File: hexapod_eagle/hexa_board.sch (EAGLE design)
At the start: 38 parts

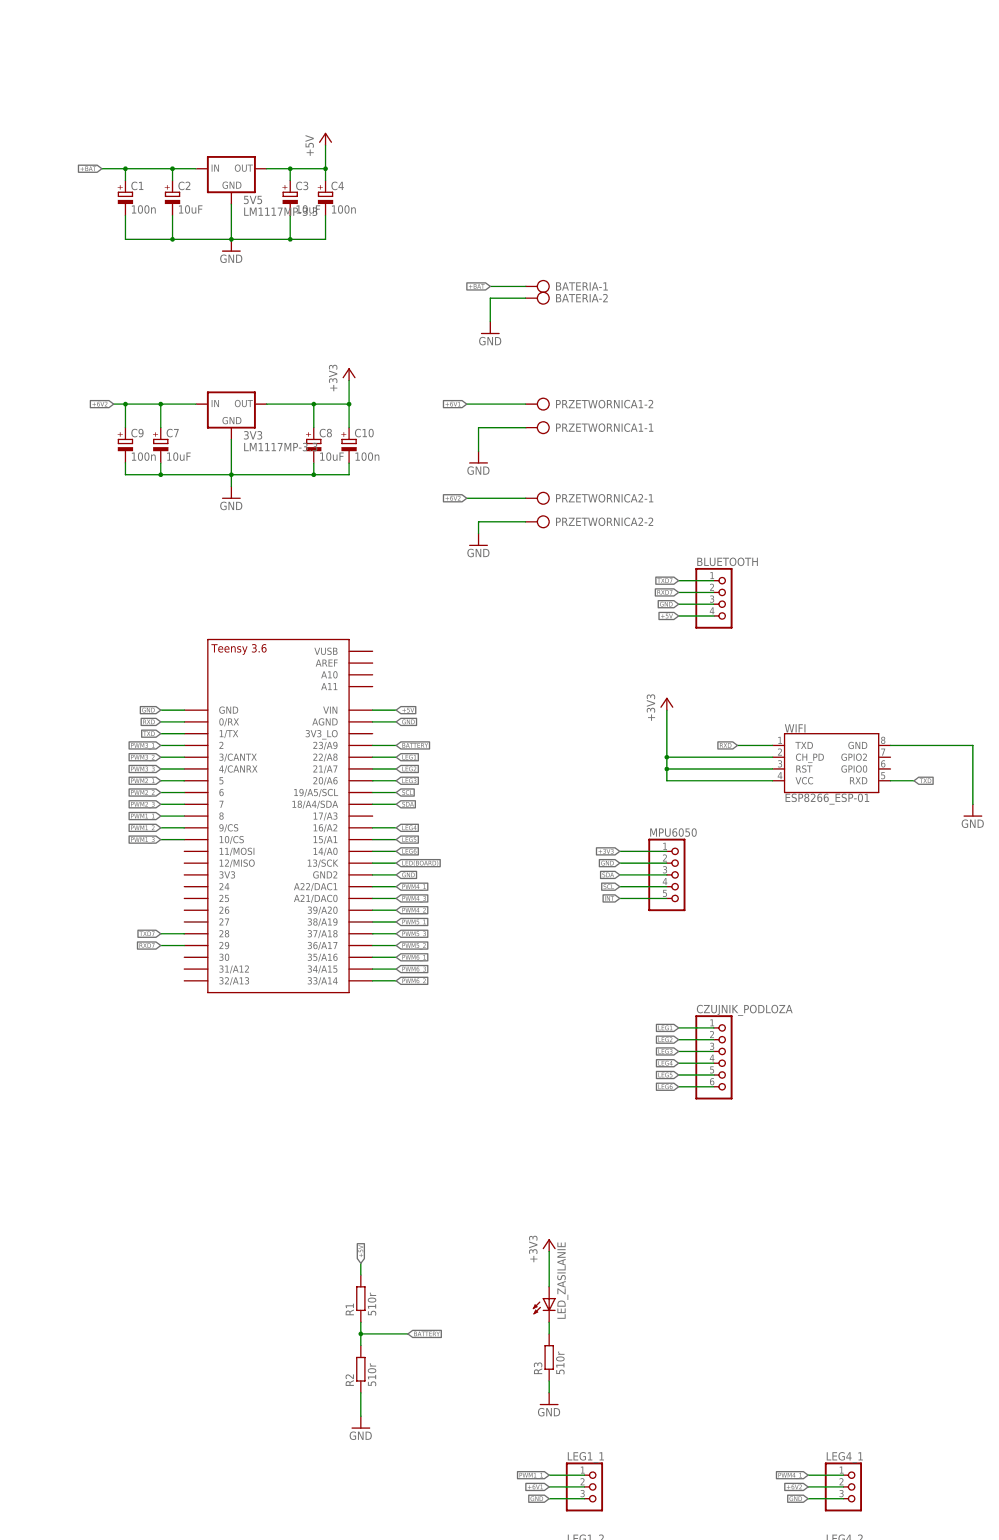
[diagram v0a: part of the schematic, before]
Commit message: Hexapod board v2
Changelog:
-new package for voltage regulator
-supply for ground sensor
-fix voltage sensor
-second battery voltage sensor
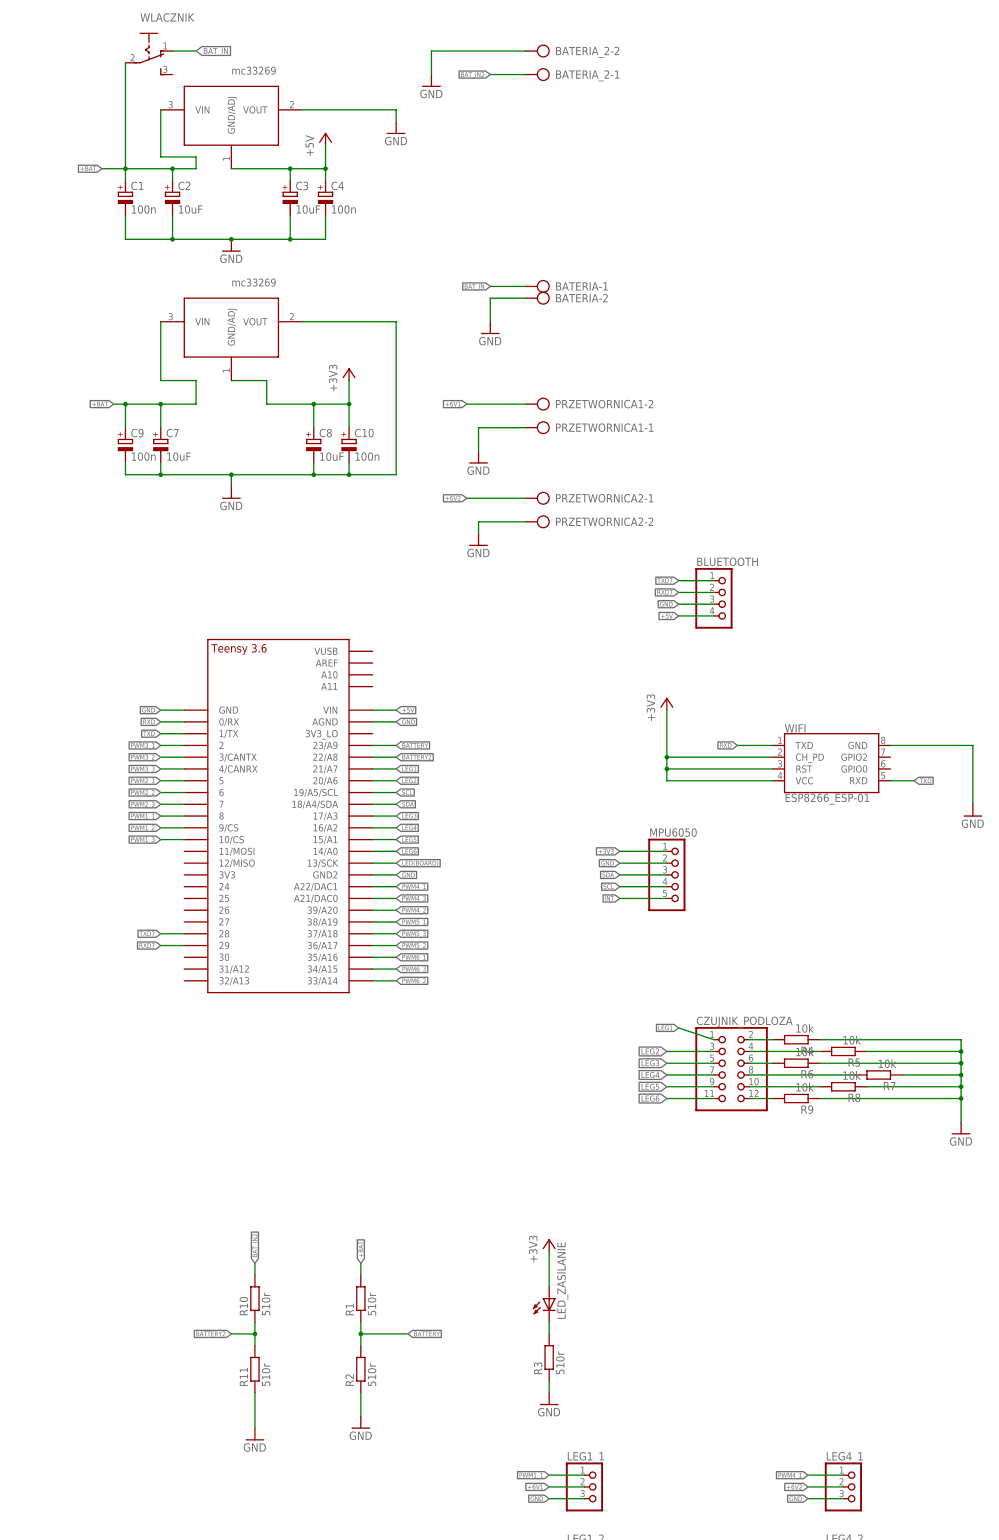
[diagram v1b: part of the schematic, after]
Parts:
- removed 3V3, 5V5: LM1117MP-3.3, lm1117_10:LM1117MP-3.3
- added 3V, 5V: MC33269, mc33269:MC33269
- added BATERIA_2: (no value), con-ptr500:AK300/2
- added R10, R11: 510r, rcl:R-EU_R0805
- added R4, R5, R6, R7, R8, R9: 10k, rcl:R-EU_R0805
- added WLACZNIK: (no value), switch:255SB
- CZUJNIK_PODLOZA: device pinhead:PINHD-1X6 -> pinhead:PINHD-2X6
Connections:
- new net BATTERY2: R10.1, R11.2, TEENSY41.22/A8
- new net BAT_IN: BATERIA-1.KL, WLACZNIK.O
- new net BAT_IN2: BATERIA_2-1.KL, R10.2
- new net N$1: CZUJNIK_PODLOZA.2, R4.2
- new net N$2: CZUJNIK_PODLOZA.4, R5.2
- new net N$3: CZUJNIK_PODLOZA.6, R6.2
- new net N$5: CZUJNIK_PODLOZA.8, R7.2
- new net N$6: CZUJNIK_PODLOZA.10, R8.2
- new net N$7: CZUJNIK_PODLOZA.12, R9.2
- net +3V3: now also 3V.GND/ADJ; no longer 3V3.OUT
- net +5V: now also 5V.GND/ADJ; no longer 5V5.OUT, R1.2
- net +6V2: no longer 3V3.IN, C7.+, C9.+
- net +BAT: now also 3V.VIN, 5V.VIN, C7.+, C9.+, R1.2, WLACZNIK.P; no longer 5V5.IN, BATERIA-1.KL
- net GND: now also 3V.VOUT, 5V.VOUT, BATERIA_2-2.KL, R11.1, R4.1, R5.1, R6.1, R7.1, R8.1, R9.1; no longer 3V3.GND, 5V5.GND
- net LEG1: now also TEENSY41.21/A7; no longer TEENSY41.22/A8
- net LEG2: now also CZUJNIK_PODLOZA.3, TEENSY41.20/A6; no longer CZUJNIK_PODLOZA.2, TEENSY41.21/A7
- net LEG3: now also CZUJNIK_PODLOZA.5, TEENSY41.17/A3; no longer CZUJNIK_PODLOZA.3, TEENSY41.20/A6
- net LEG4: now also CZUJNIK_PODLOZA.7; no longer CZUJNIK_PODLOZA.4
- net LEG5: now also CZUJNIK_PODLOZA.9; no longer CZUJNIK_PODLOZA.5
- net LEG6: now also CZUJNIK_PODLOZA.11; no longer CZUJNIK_PODLOZA.6

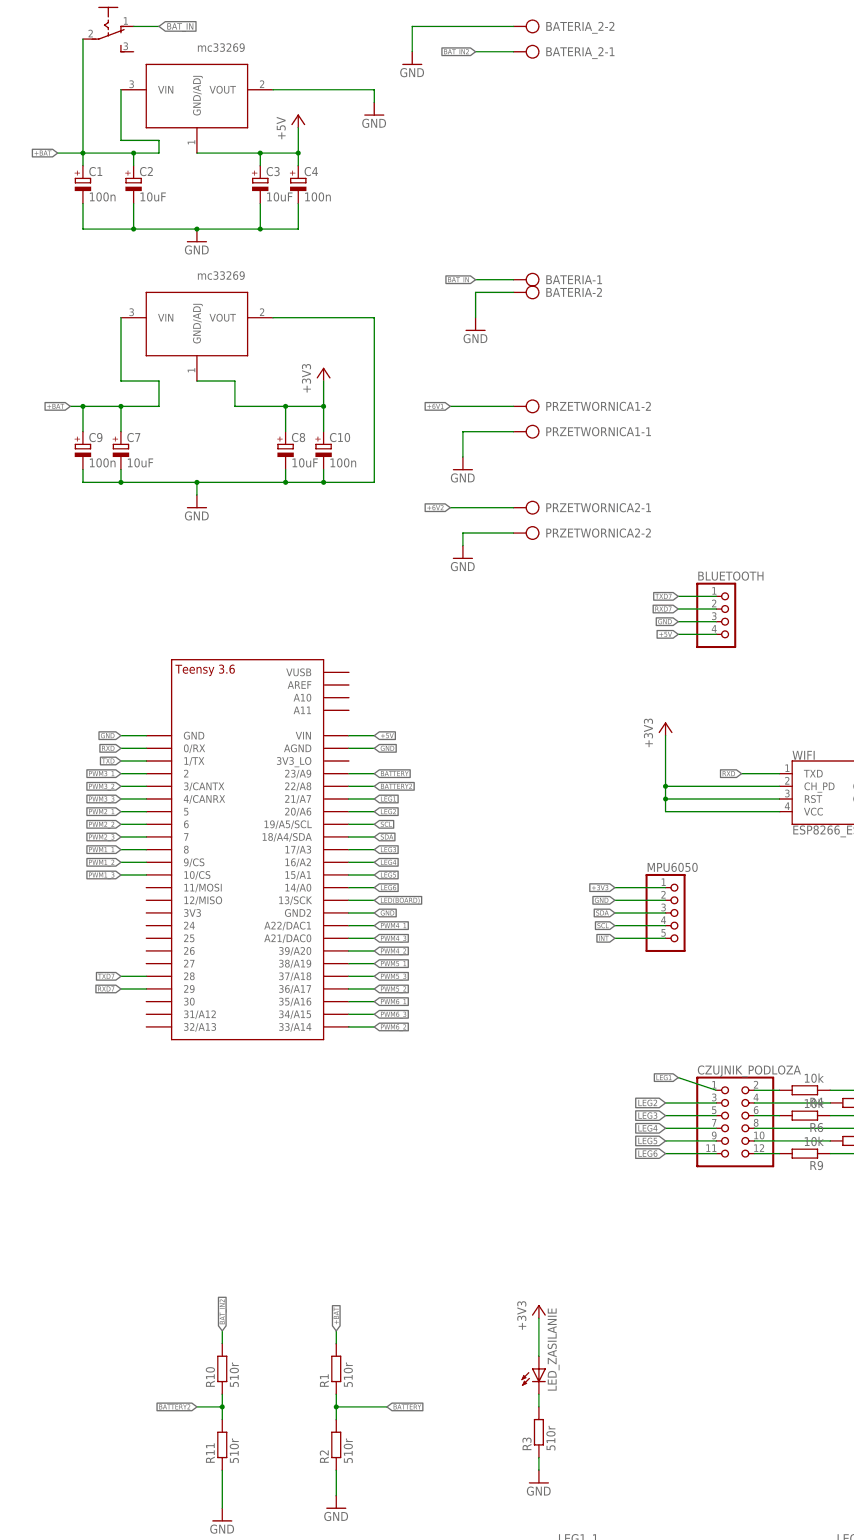
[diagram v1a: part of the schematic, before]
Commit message: Board v2
Changelog:
-on/off swich for power mcu(was in last update)
-add 2 leds for comunication
-some positions changes
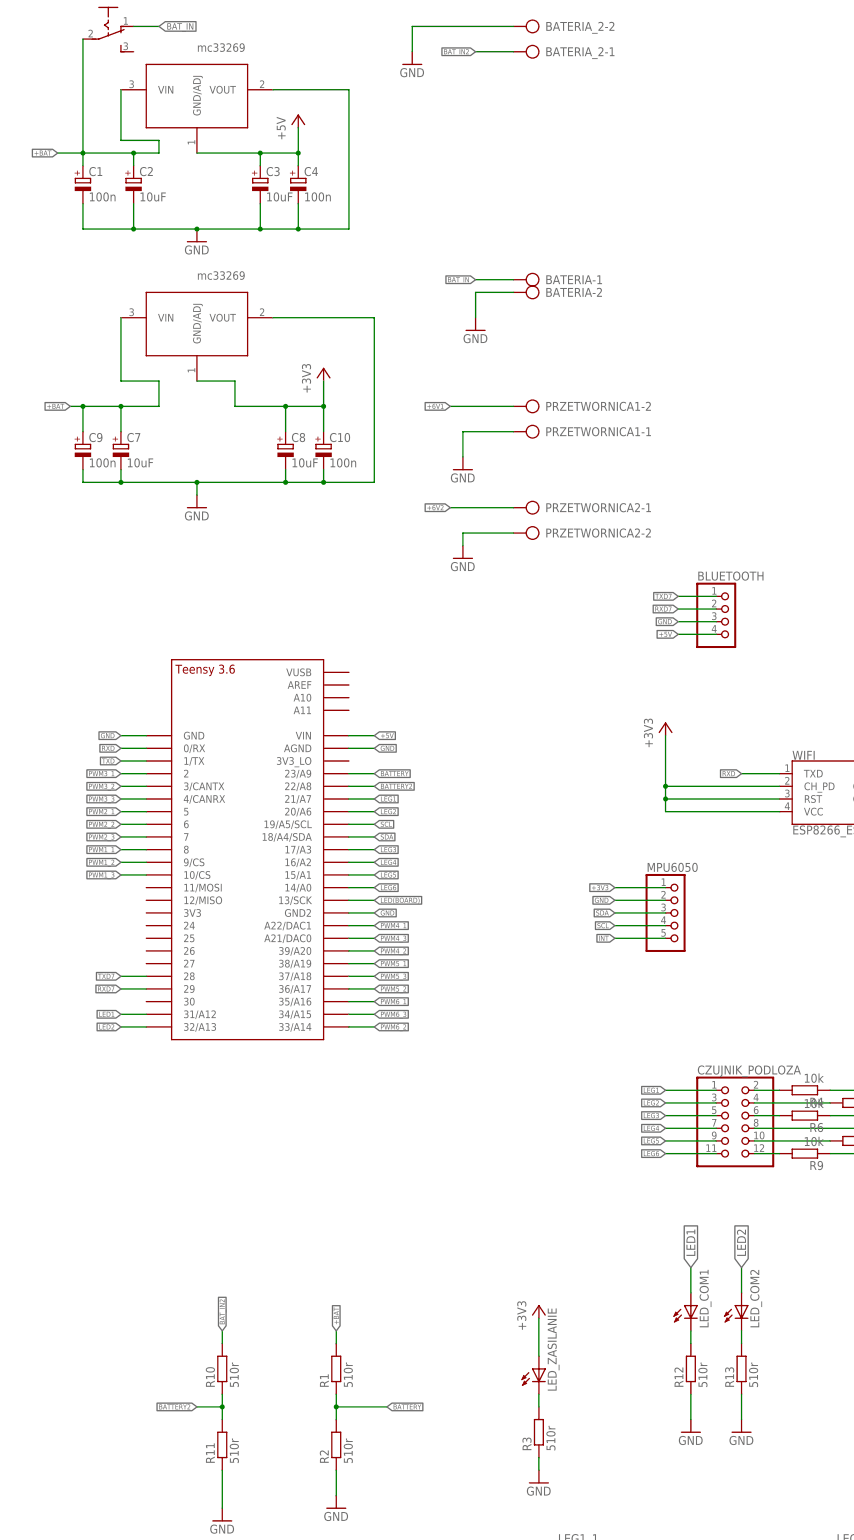
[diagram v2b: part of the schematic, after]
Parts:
- added LED_COM1, LED_COM2: (no value), led:LEDSML0805
- added R12, R13: 510r, rcl:R-EU_R0805
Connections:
- new net LED1: LED_COM1.A, TEENSY41.31/A12
- new net LED2: LED_COM2.A, TEENSY41.32/A13
- new net N$8: LED_COM1.C, R12.2
- new net N$9: LED_COM2.C, R13.2
- net GND: now also R12.1, R13.1
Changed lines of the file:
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@@
 <part name="GND7" library="supply1" deviceset="GND" device=""/>
 <part name="5V" library="mc33269" deviceset="MC33269" device=""/>
-<part name="GND9" library="supply1" deviceset="GND" device=""/>
 <part name="3V" library="mc33269" deviceset="MC33269" device=""/>
+<part name="R12" library="rcl" deviceset="R-EU_" device="R0805" value="510r"/>
+<part name="R13" library="rcl" deviceset="R-EU_" device="R0805" value="510r"/>
+<part name="LED_COM1" library="led" deviceset="LED" device="SML0805"/>
+<part name="LED_COM2" library="led" deviceset="LED" device="SML0805"/>
+<part name="GND10" library="supply1" deviceset="GND" device=""/>
+<part name="GND14" library="supply1" deviceset="GND" device=""/>
 </parts>
 <sheets>
@@
 <instance part="GND7" gate="1" x="30.48" y="-5.08"/>
 <instance part="5V" gate="G$1" x="27.94" y="271.78"/>
-<instance part="GND9" gate="1" x="60.96" y="276.86"/>
 <instance part="3V" gate="G$1" x="27.94" y="226.06"/>
+<instance part="R12" gate="G$1" x="124.46" y="25.4" rot="R90"/>
+<instance part="R13" gate="G$1" x="134.62" y="25.4" rot="R90"/>
+<instance part="LED_COM1" gate="G$1" x="124.46" y="38.1"/>
+<instance part="LED_COM2" gate="G$1" x="134.62" y="38.1"/>
+<instance part="GND10" gate="1" x="124.46" y="12.7"/>
+<instance part="GND14" gate="1" x="134.62" y="12.7"/>
 </instances>
 <busses>
@@
 <wire x1="45.72" y1="254" x2="45.72" y2="259.08" width="0.1524" layer="91"/>
 <junction x="38.1" y="254"/>
+<wire x1="45.72" y1="254" x2="55.88" y2="254" width="0.1524" layer="91"/>
+<junction x="45.72" y="254"/>
+<pinref part="5V" gate="G$1" pin="VOUT"/>
+<wire x1="40.64" y1="281.94" x2="55.88" y2="281.94" width="0.1524" layer="91"/>
+<wire x1="55.88" y1="254" x2="55.88" y2="281.94" width="0.1524" layer="91"/>
 </segment>
 <segment>
@@
 </segment>
 <segment>
-<pinref part="5V" gate="G$1" pin="VOUT"/>
-<pinref part="GND9" gate="1" pin="GND"/>
-<wire x1="40.64" y1="281.94" x2="60.96" y2="281.94" width="0.1524" layer="91"/>
-<wire x1="60.96" y1="281.94" x2="60.96" y2="279.4" width="0.1524" layer="91"/>
+<pinref part="R12" gate="G$1" pin="1"/>
+<pinref part="GND10" gate="1" pin="GND"/>
+<wire x1="124.46" y1="20.32" x2="124.46" y2="15.24" width="0.1524" layer="91"/>
+</segment>
+<segment>
+<pinref part="R13" gate="G$1" pin="1"/>
+<pinref part="GND14" gate="1" pin="GND"/>
+<wire x1="134.62" y1="20.32" x2="134.62" y2="15.24" width="0.1524" layer="91"/>
 </segment>
 </net>
@@
 <pinref part="CZUJNIK_PODLOZA" gate="A" pin="11"/>
 <wire x1="129.54" y1="68.58" x2="119.38" y2="68.58" width="0.1524" layer="91"/>
-<label x="119.38" y="68.58" size="1.27" layer="95" rot="R180" xref="yes"/>
+<label x="119.38" y="68.58" size="1.016" layer="95" rot="R180" xref="yes"/>
 </segment>
 </net>
@@
 <pinref part="CZUJNIK_PODLOZA" gate="A" pin="9"/>
 <wire x1="129.54" y1="71.12" x2="119.38" y2="71.12" width="0.1524" layer="91"/>
-<label x="119.38" y="71.12" size="1.27" layer="95" rot="R180" xref="yes"/>
+<label x="119.38" y="71.12" size="1.016" layer="95" rot="R180" xref="yes"/>
 </segment>
 </net>
@@
 <pinref part="CZUJNIK_PODLOZA" gate="A" pin="7"/>
 <wire x1="129.54" y1="73.66" x2="119.38" y2="73.66" width="0.1524" layer="91"/>
-<label x="119.38" y="73.66" size="1.27" layer="95" rot="R180" xref="yes"/>
+<label x="119.38" y="73.66" size="1.016" layer="95" rot="R180" xref="yes"/>
 </segment>
 </net>
@@
 <segment>
 <pinref part="CZUJNIK_PODLOZA" gate="A" pin="1"/>
-<wire x1="129.54" y1="81.28" x2="121.92" y2="83.82" width="0.1524" layer="91"/>
-<label x="121.92" y="83.82" size="1.016" layer="95" rot="R180" xref="yes"/>
+<wire x1="129.54" y1="81.28" x2="119.38" y2="81.28" width="0.1524" layer="91"/>
+<label x="119.38" y="81.28" size="1.016" layer="95" rot="R180" xref="yes"/>
 </segment>
 <segment>
@@
 <pinref part="CZUJNIK_PODLOZA" gate="A" pin="3"/>
 <wire x1="129.54" y1="78.74" x2="119.38" y2="78.74" width="0.1524" layer="91"/>
-<label x="119.38" y="78.74" size="1.27" layer="95" rot="R180" xref="yes"/>
+<label x="119.38" y="78.74" size="1.016" layer="95" rot="R180" xref="yes"/>
 </segment>
 <segment>
@@
 <pinref part="CZUJNIK_PODLOZA" gate="A" pin="5"/>
 <wire x1="129.54" y1="76.2" x2="119.38" y2="76.2" width="0.1524" layer="91"/>
-<label x="119.38" y="76.2" size="1.27" layer="95" rot="R180" xref="yes"/>
+<label x="119.38" y="76.2" size="1.016" layer="95" rot="R180" xref="yes"/>
 </segment>
 <segment>
@@
 </segment>
 </net>
+<net name="N$8" class="0">
+<segment>
+<pinref part="LED_COM1" gate="G$1" pin="C"/>
+<pinref part="R12" gate="G$1" pin="2"/>
+<wire x1="124.46" y1="33.02" x2="124.46" y2="30.48" width="0.1524" layer="91"/>
+</segment>
+</net>
+<net name="N$9" class="0">
+<segment>
+<pinref part="LED_COM2" gate="G$1" pin="C"/>
+<pinref part="R13" gate="G$1" pin="2"/>
+<wire x1="134.62" y1="33.02" x2="134.62" y2="30.48" width="0.1524" layer="91"/>
+</segment>
+</net>
+<net name="LED1" class="0">
+<segment>
+<pinref part="LED_COM1" gate="G$1" pin="A"/>
+<wire x1="124.46" y1="40.64" x2="124.46" y2="45.72" width="0.1524" layer="91"/>
+<label x="124.46" y="45.72" size="1.778" layer="95" rot="R90" xref="yes"/>
+</segment>
+<segment>
+<pinref part="TEENSY41" gate="G$1" pin="31/A12"/>
+<wire x1="15.24" y1="96.52" x2="10.16" y2="96.52" width="0.1524" layer="91"/>
+<label x="10.16" y="96.52" size="1.016" layer="95" rot="R180" xref="yes"/>
+</segment>
+</net>
+<net name="LED2" class="0">
+<segment>
+<pinref part="LED_COM2" gate="G$1" pin="A"/>
+<wire x1="134.62" y1="40.64" x2="134.62" y2="45.72" width="0.1524" layer="91"/>
+<label x="134.62" y="45.72" size="1.778" layer="95" rot="R90" xref="yes"/>
+</segment>
+<segment>
+<pinref part="TEENSY41" gate="G$1" pin="32/A13"/>
+<wire x1="15.24" y1="93.98" x2="10.16" y2="93.98" width="0.1524" layer="91"/>
+<label x="10.16" y="93.98" size="1.016" layer="95" rot="R180" xref="yes"/>
+</segment>
+</net>
